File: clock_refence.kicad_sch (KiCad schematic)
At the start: 52 parts, among them J204 REFOUT_AUX_P, J205 REFOUT_AUX_N, J206 RFShield_TwoPieces, J207 REFOUT, J209 DNP, T202 TC2-1T+, U201 Si53301, U202 XC6204B33

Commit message: Footprint changes
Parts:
- C219, C233: footprint Capacitor_SMD:CP_Elec_6.3x7.7 -> Capacitor_SMD:CP_Elec_6.3x5.8; symbol Device:C_Polarized_Small -> petr:CP_47uF_35V
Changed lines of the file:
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@@
     (pin "5")
   )
-  (symbol (lib_id "Device:C_Polarized_Small") (at 20.32 181.61 0) (unit 1)
+  (symbol (lib_id "petr:CP_47uF_35V") (at 20.32 181.61 0) (unit 1)
     (in_bom yes) (on_board yes)
     (property "Reference" "C219" (id 0) (at 18.1609 180.4606 0)
@@
       (effects (font (size 1.27 1.27)) (justify right))
     )
-    (property "Footprint" "Capacitor_SMD:CP_Elec_6.3x7.7" (id 2) (at 20.32 181.61 0)
+    (property "Footprint" "Capacitor_SMD:CP_Elec_6.3x5.8" (id 2) (at 20.32 181.61 0)
       (effects (font (size 1.27 1.27)) hide)
     )
-    (property "Datasheet" "~" (id 3) (at 20.32 181.61 0)
+    (property "Datasheet" "http://www.samwha.com/electric/product/list_pdf2/CK.pdf" (id 3) (at 20.32 181.61 0)
       (effects (font (size 1.27 1.27)) hide)
     )
@@
     (pin "3")
   )
-  (symbol (lib_id "Device:C_Polarized_Small") (at 111.76 181.61 0) (unit 1)
+  (symbol (lib_id "petr:CP_47uF_35V") (at 111.76 181.61 0) (unit 1)
     (in_bom yes) (on_board yes)
     (property "Reference" "C233" (id 0) (at 113.9191 180.4606 0)
@@
       (effects (font (size 1.27 1.27)) (justify left))
     )
-    (property "Footprint" "Capacitor_SMD:CP_Elec_6.3x7.7" (id 2) (at 111.76 181.61 0)
+    (property "Footprint" "Capacitor_SMD:CP_Elec_6.3x5.8" (id 2) (at 111.76 181.61 0)
       (effects (font (size 1.27 1.27)) hide)
     )
-    (property "Datasheet" "~" (id 3) (at 111.76 181.61 0)
+    (property "Datasheet" "http://www.samwha.com/electric/product/list_pdf2/CK.pdf" (id 3) (at 111.76 181.61 0)
       (effects (font (size 1.27 1.27)) hide)
     )

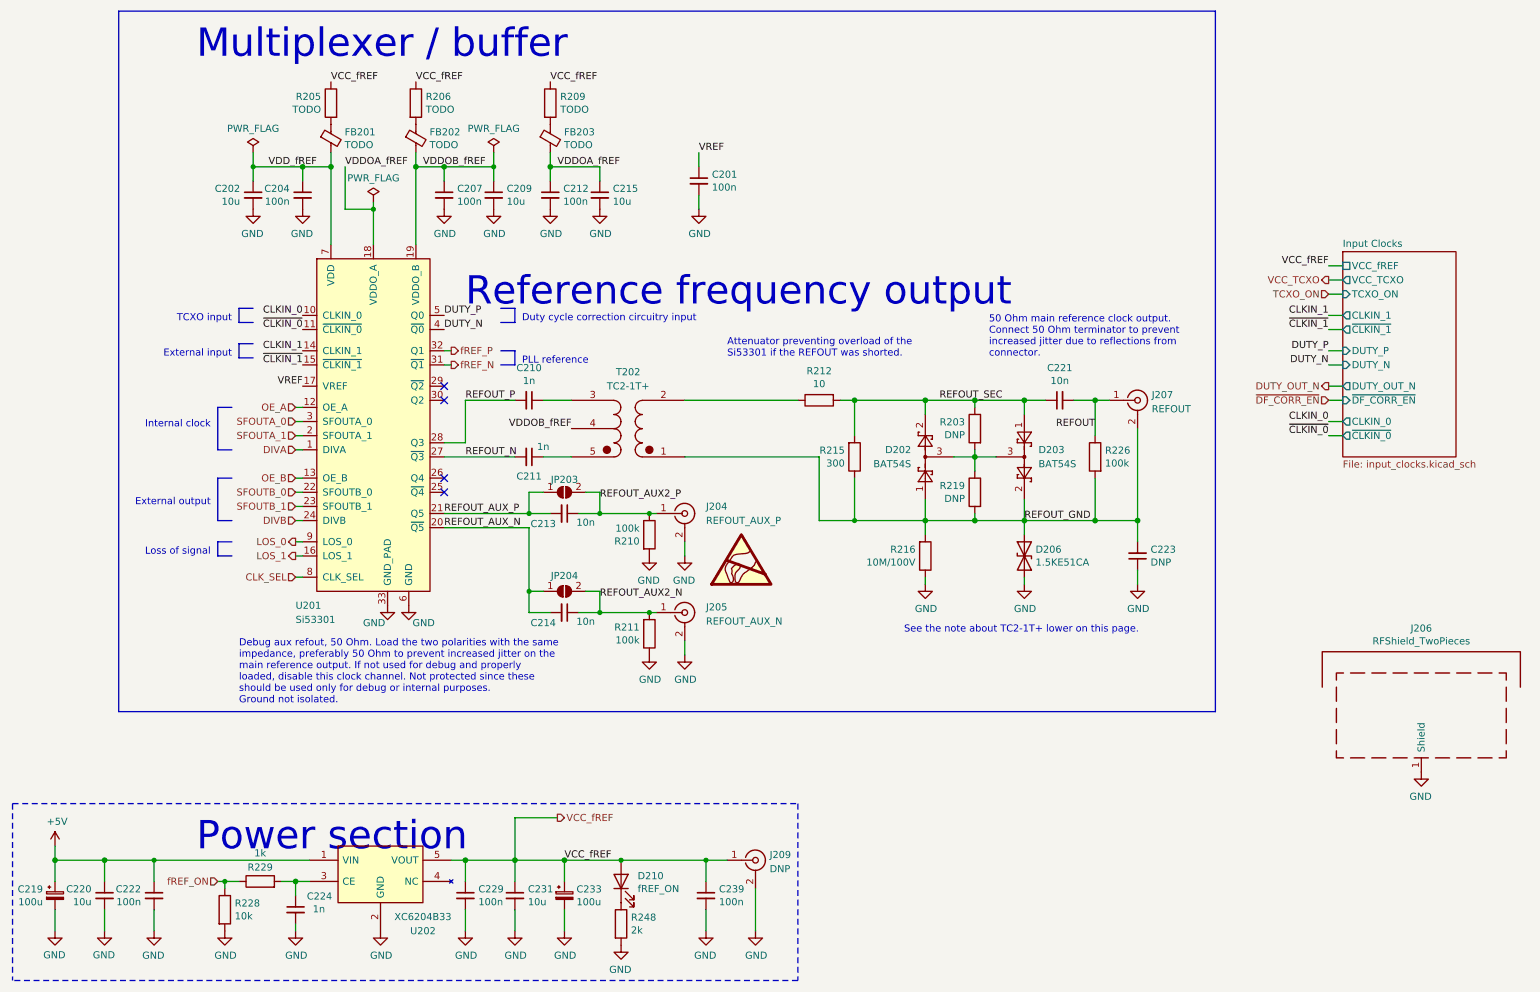
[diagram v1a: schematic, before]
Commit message: Remade and simplified AUX/EXT section.
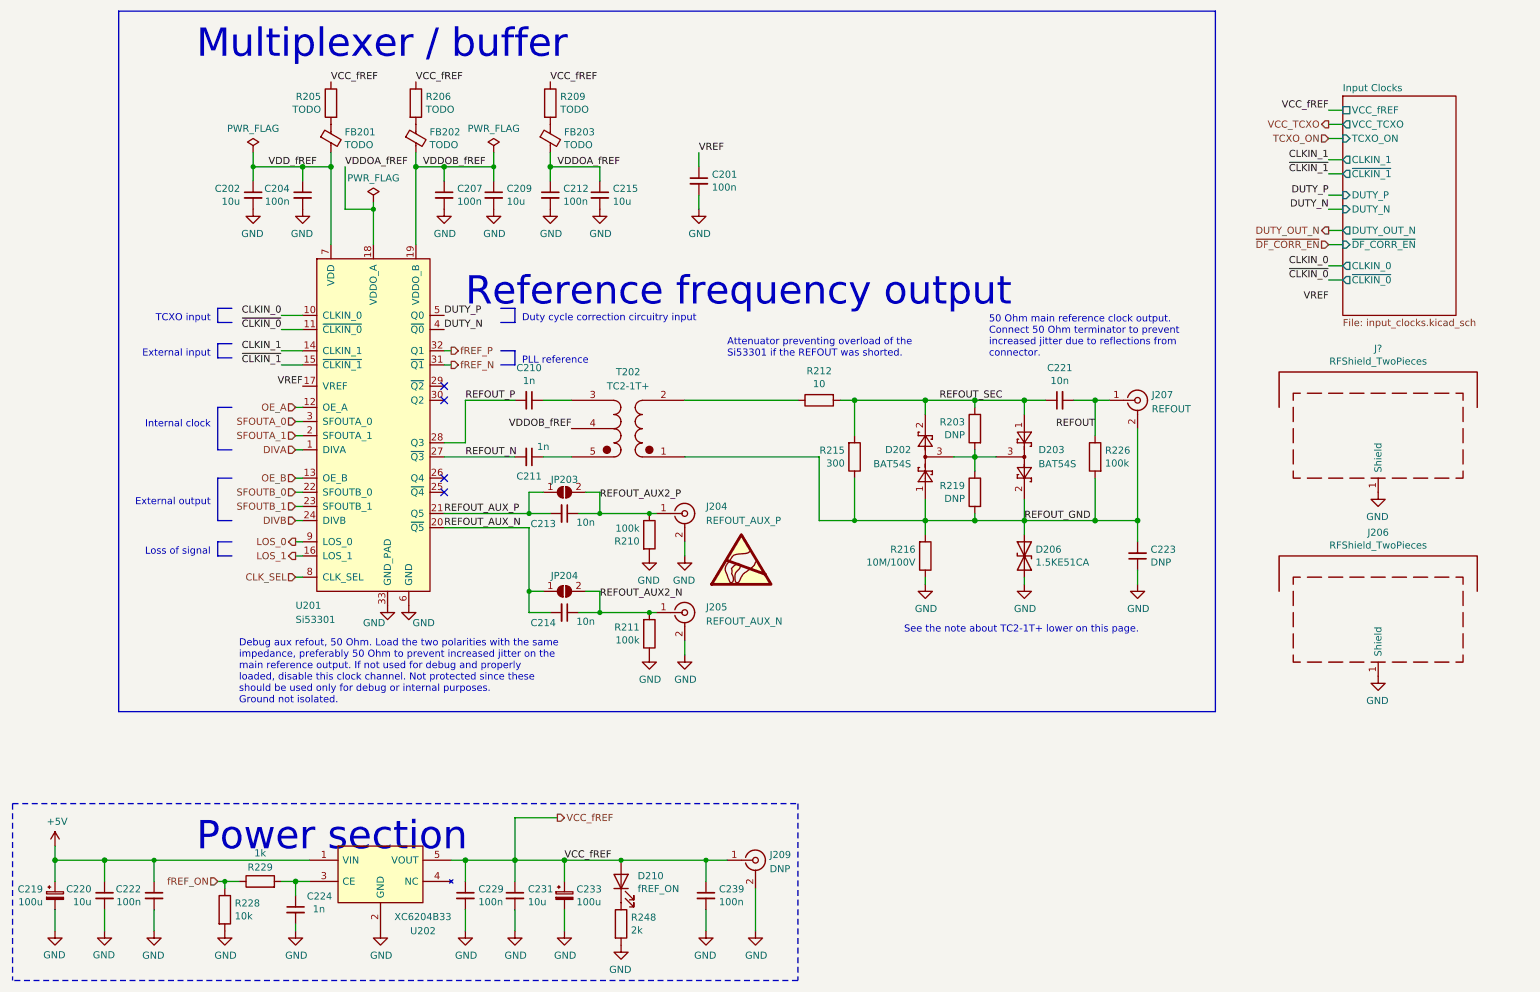
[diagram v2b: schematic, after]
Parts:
- added J?: RFShield_TwoPieces, RF_Shielding:Laird_Technologies_BMI-S-205-F_38.10x25.40mm, symbol Device:RFShield_TwoPieces
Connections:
- net GND: now also J?.1 (Shield)
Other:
- moved on the sheet: J206

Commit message: Fixes.
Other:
- title: Generator 0.0125 - 6.4 GHz (0.02 - 9.8 GHz) -> Generator 0.0125 - 6.4 GHz (or up to 20 GHz)
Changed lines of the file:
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@@
   (paper "A4")
   (title_block
-    (title "Generator 0.0125 - 6.4 GHz (0.02 - 9.8 GHz)")
-    (date "2021-11-13")
-    (rev "211113-001")
+    (title "Generator 0.0125 - 6.4 GHz (or up to 20 GHz)")
+    (date "2021-12-30")
+    (rev "211230-001")
     (company "Petr Polasek")
-    (comment 1 "001, 2021-11-13 09:38")
-    (comment 2 "TCXO / external input, LMX2572/LMX2592")
-    (comment 3 "Dual channel symmetric outputs")
+    (comment 1 "001, 2021-12-30 00:50")
+    (comment 2 "TCXO / external input")
+    (comment 3 "LMX2572 (6.4 GHz) / LMX2592 (9.8GHz) / LMX2594 (15 GHz) / LMX2595 (20 GHz)")
   )
   (junction (at 63.5 179.07) (diameter 1.016) (color 0 0 0 0)

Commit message: Schematic ready for impoting changes into PCB.
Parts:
- gave numbers to parts that had none: 1
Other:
- sheet Input Clocks ports: added VREF; removed none
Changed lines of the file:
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@@
     (rev "211230-001")
     (company "Petr Polasek")
-    (comment 1 "001, 2021-12-30 00:50")
+    (comment 1 "001, 2021-12-30 01:03")
     (comment 2 "TCXO / external input")
     (comment 3 "LMX2572 (6.4 GHz) / LMX2592 (9.8GHz) / LMX2594 (15 GHz) / LMX2595 (20 GHz)")
@@
   (wire (pts (xy 185.42 93.98) (xy 185.42 92.71))
     (stroke (width 0) (type solid) (color 0 0 0 0))
+  )
+  (wire (pts (xy 248.92 74.93) (xy 251.46 74.93))
+    (stroke (width 0) (type default) (color 0 0 0 0))
   )
   (wire (pts (xy 111.76 175.26) (xy 121.92 175.26))
@@
   (symbol (lib_id "Device:RFShield_TwoPieces") (at 257.81 99.06 0) (unit 1)
     (in_bom yes) (on_board yes)
-    (property "Reference" "J?" (id 0) (at 257.81 83.4198 0))
+    (property "Reference" "J210" (id 0) (at 257.81 83.4198 0))
     (property "Value" "RFShield_TwoPieces" (id 1) (at 257.81 85.7185 0))
     (property "Footprint" "RF_Shielding:Laird_Technologies_BMI-S-205-F_38.10x25.40mm" (id 2) (at 257.81 101.6 0)
@@
   (symbol (lib_id "power:GND") (at 257.81 109.22 0) (mirror y) (unit 1)
     (in_bom yes) (on_board yes)
-    (property "Reference" "#PWR?" (id 0) (at 257.81 115.57 0)
+    (property "Reference" "#PWR0113" (id 0) (at 257.81 115.57 0)
       (effects (font (size 1.27 1.27)) hide)
     )
@@
       (effects (font (size 1.27 1.27)) (justify left))
     )
+    (pin "VREF" passive (at 251.46 74.93 180)
+      (effects (font (size 1.27 1.27)) (justify left))
+    )

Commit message: Synchronised PCB and schematic.
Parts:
- removed D206: 1.5KE51CA, Diode_THT:D_DO-201AE_P15.24mm_Horizontal, symbol Diode:1.5KExxCA
- added D201: SMAJ48CA, Diode_SMD_AKL:D_SMA_TVS, symbol Diode_TVS_AKL:SMAJ48CA
- J207: footprint petr_kicad:SMA_rosenberger_hybrid -> petr:SMA_rosenberger_hybrid
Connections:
- net GND: now also D201.1 (K)
- net REFOUT_GND: now also D201.2 (A)
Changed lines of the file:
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@@
     (pin "1")
-  )
-  (symbol (lib_id "Diode:1.5KExxCA") (at 194.31 120.65 270) (unit 1)
-    (in_bom yes) (on_board yes)
-    (property "Reference" "D206" (id 0) (at 196.3166 119.4816 90)
-      (effects (font (size 1.27 1.27)) (justify left))
-    )
-    (property "Value" "1.5KE51CA" (id 1) (at 196.3166 121.793 90)
-      (effects (font (size 1.27 1.27)) (justify left))
-    )
-    (property "Footprint" "Diode_THT:D_DO-201AE_P15.24mm_Horizontal" (id 2) (at 189.23 120.65 0)
-      (effects (font (size 1.27 1.27)) hide)
-    )
-    (property "Datasheet" "https://www.vishay.com/docs/88301/15ke.pdf" (id 3) (at 194.31 120.65 0)
-      (effects (font (size 1.27 1.27)) hide)
-    )
-    (pin "1")
-    (pin "2")
   )
   (symbol (lib_id "power:GND") (at 194.31 125.73 0) (unit 1)
@@
     (pin "2")
   )
+  (symbol (lib_id "Diode_TVS_AKL:SMAJ48CA") (at 194.31 120.65 90) (unit 1)
+    (in_bom yes) (on_board yes) (fields_autoplaced)
+    (property "Reference" "D201" (id 0) (at 196.85 119.3799 90)
+      (effects (font (size 1.27 1.27)) (justify right))
+    )
+    (property "Value" "SMAJ48CA" (id 1) (at 196.85 121.9199 90)
+      (effects (font (size 1.27 1.27)) (justify right))
+    )
+    (property "Footprint" "Diode_SMD_AKL:D_SMA_TVS" (id 2) (at 194.31 120.65 0)
+      (effects (font (size 1.27 1.27)) hide)
+    )
+    (property "Datasheet" "https://www.tme.eu/Document/dbc72d81c249fe51b6ab42300e8e06d0/SMAJ_ser.pdf" (id 3) (at 194.31 120.65 0)
+      (effects (font (size 1.27 1.27)) hide)
+    )
+    (pin "1")
+    (pin "2")
+  )
   (symbol (lib_id "Device:R") (at 185.42 97.79 0) (mirror y) (unit 1)
     (in_bom yes) (on_board yes)
@@
       (effects (font (size 1.27 1.27)) (justify left))
     )
-    (property "Footprint" "petr_kicad:SMA_rosenberger_hybrid" (id 2) (at 214.63 92.71 0)
-      (effects (font (size 1.27 1.27)) hide)
-    )
+    (property "Footprint" "petr:SMA_rosenberger_hybrid" (id 2) (at 214.63 92.71 0)
+      (effects (font (size 1.27 1.27)) hide)
+    )

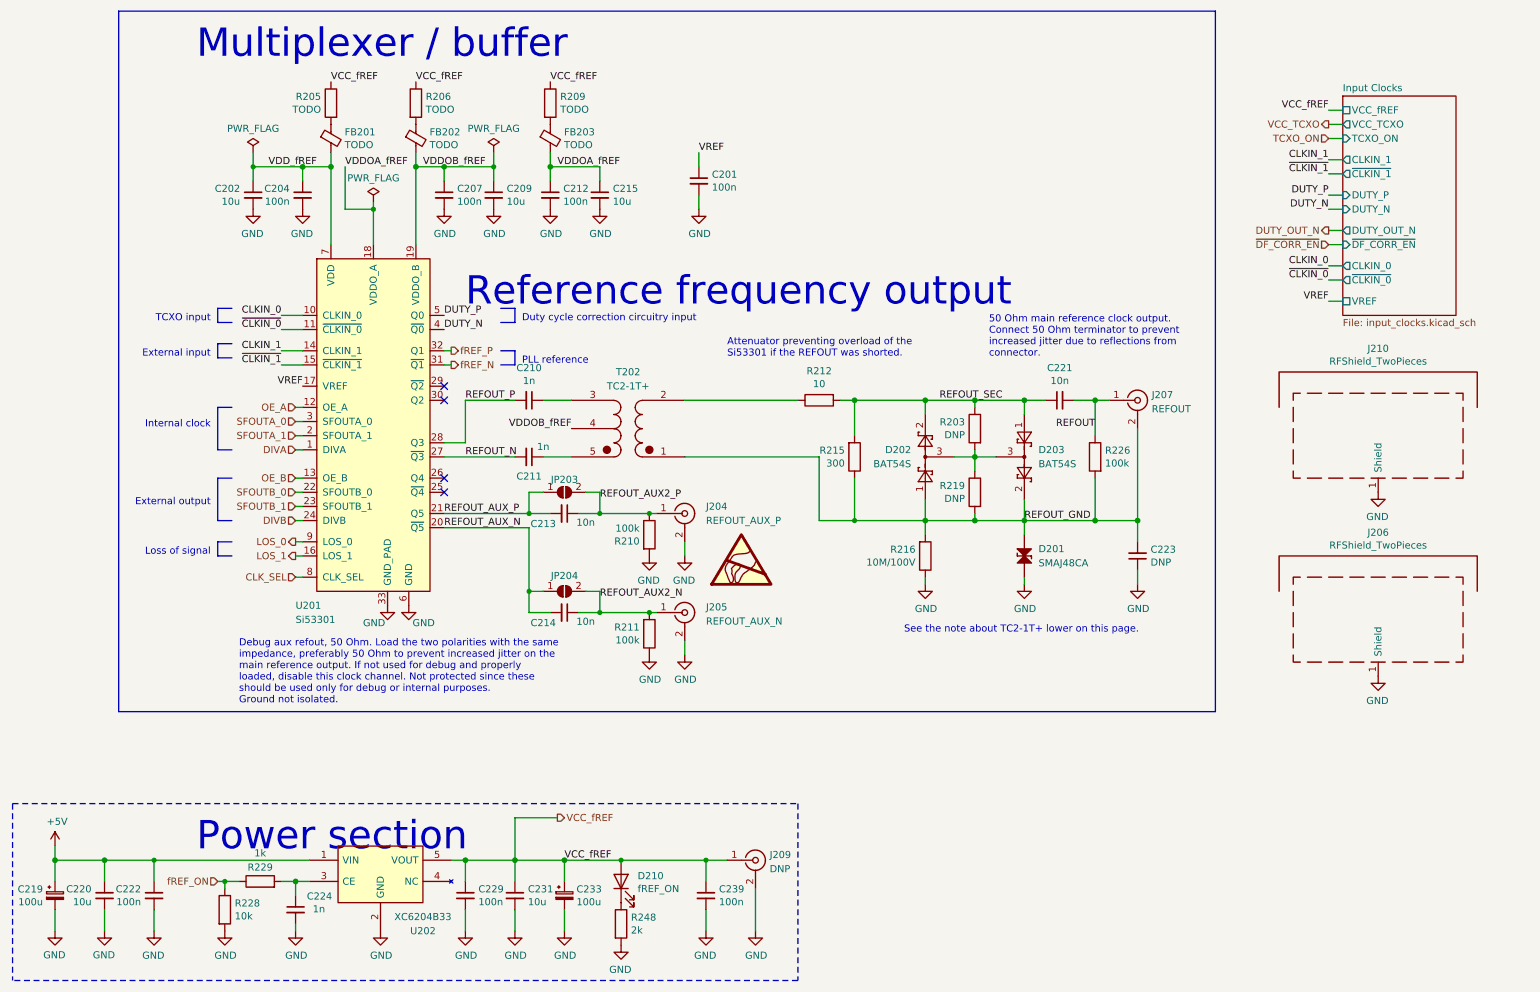
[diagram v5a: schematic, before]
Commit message: Minor improvements and fixes to schematic, added high current LDO needed for high frequency PLLs.
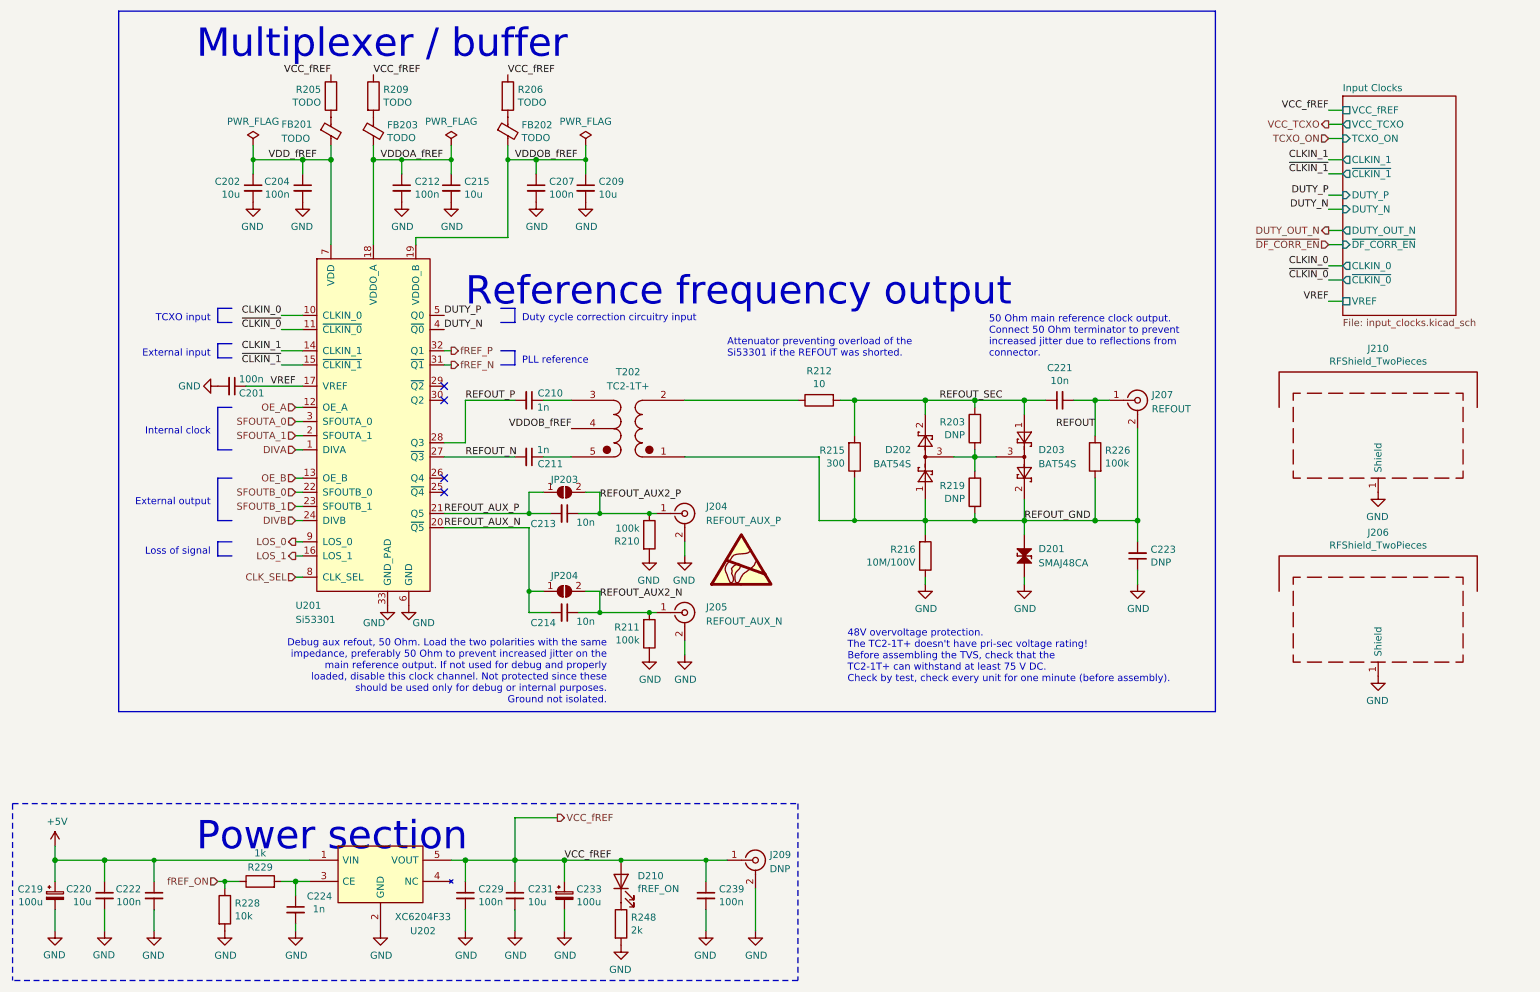
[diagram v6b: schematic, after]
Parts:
- U202: value XC6204B33 -> XC6204F33; symbol petr:XC6204B33 -> petr:XC6204F33
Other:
- note added: "48V overvoltage protection. The TC2-1T+ doesn't have pri-sec voltage rating! Before assembling the TVS, check that the TC2-1T+ can withstand at least 75 V DC. Check by test, check every unit for one minute (before assembly)."
- note removed: "See the note about TC2-1T+ lower on this page."
- moved on the sheet: C201, C202, C204, C207, C209, C212, C215, FB201, FB202, FB203, R205, R206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
